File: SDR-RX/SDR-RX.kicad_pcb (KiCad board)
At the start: 2 copper layers, 53 x 51 mm, 50 parts, among them Q1 S8050, Q2 S8050, U1 Si4734-D60-GU, U2 ESP32-WROOM-32, U3 LD1117S33TR_SOT223, Y1 32.768kHz

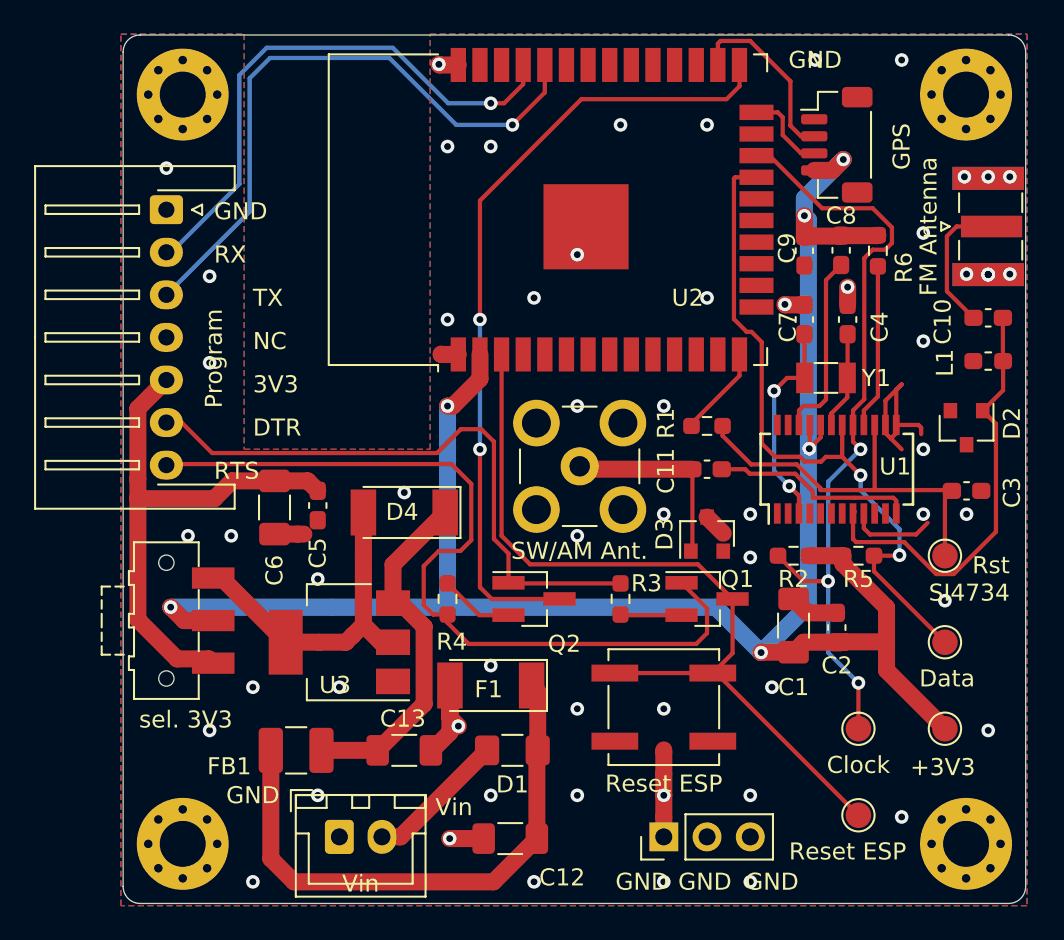
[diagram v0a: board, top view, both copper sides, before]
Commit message: changed footprint D1 & D4 due to assembly objection
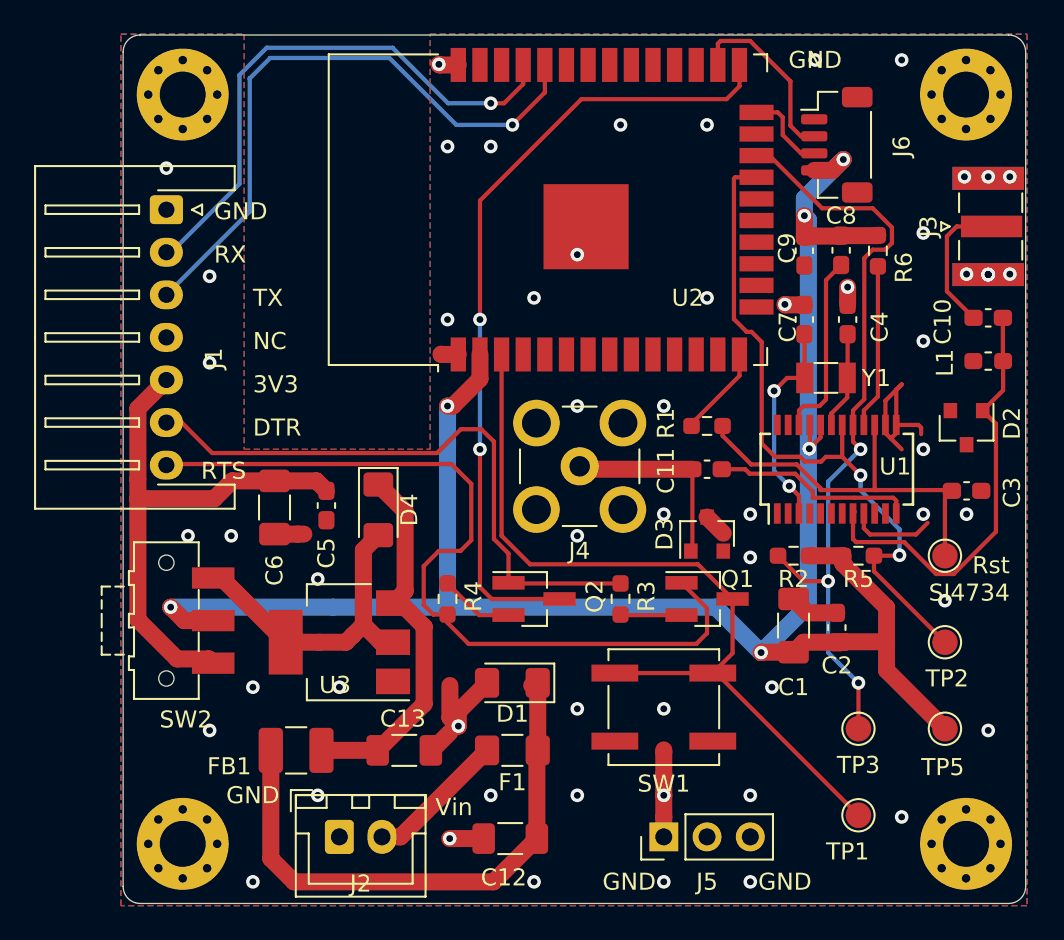
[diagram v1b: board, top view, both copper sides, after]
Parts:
- D1, D4: footprint Diode_SMD:D_MELF -> Diode_SMD:D_1206_3216Metric_Pad1.42x1.75mm_HandSolder
- J1: renamed from Program; value J1 -> Program
- J2: renamed from Vin ; value J2 -> Vin
- J3: renamed from FM Antenna; value J3 -> FM Antenna
- J4: renamed from SW/AM Ant.
- J6: renamed from GPS; value J6 -> GPS
- SW1: renamed from Reset ESP; value SW1 -> Reset ESP
- SW2: renamed from sel. 3V3 ; value SW2 -> 3V3 J5/J2
- TP1: renamed from Reset ESP
- TP4: renamed from Reset SI4734
- TP5: renamed from +3V3; value TP5 -> +3V3
- moved D4 1.53 mm to (125.2, 92.6), turned to 270 degrees
- moved D1 1.28 mm to (133.1, 102.8)
- moved C5 0.51 mm to (122.2, 92.4)
- renumbered GND to J5, Data to TP2, Clock to TP3
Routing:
- net Net-(C13-Pad1): track 20.7 -> 22.0 mm
- net Net-(C5-Pad1): track 32.0 -> 32.5 mm
- net GND: track 39.4 -> 39.8 mm, vias 60 -> 58

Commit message: changed Designator J5 to Program1 to avoid BPM/CPL missmatch on SMT assembly
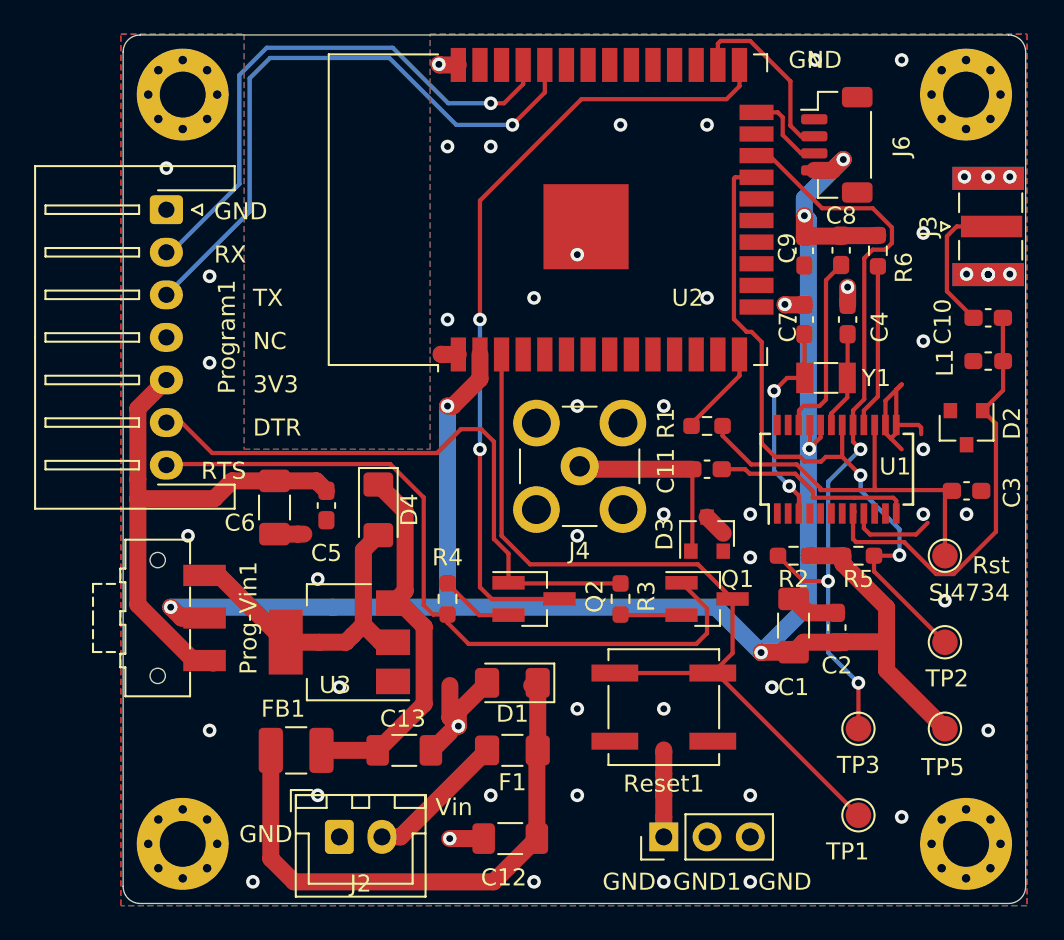
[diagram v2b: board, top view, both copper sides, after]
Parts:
- GND1: renamed from J5; value Conn_01x03_Male -> GND TP
- Prog-Vin1: renamed from SW2; value 3V3 J5/J2 -> SW2
- Program1: renamed from J1; value Program -> J1
- Reset1: renamed from SW1; value Reset ESP -> SW1
- moved Prog-Vin1 0.53 mm to (112.3, 99.0)
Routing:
- net Net-(Program1-Pad7): track 49.1 -> 44.0 mm
- net Net-(D4-Pad2): track 19.1 -> 20.8 mm
- net Net-(C5-Pad1): track 32.5 -> 31.8 mm
- net +3V3: track 118.8 -> 118.3 mm
- net GND: vias 58 -> 55

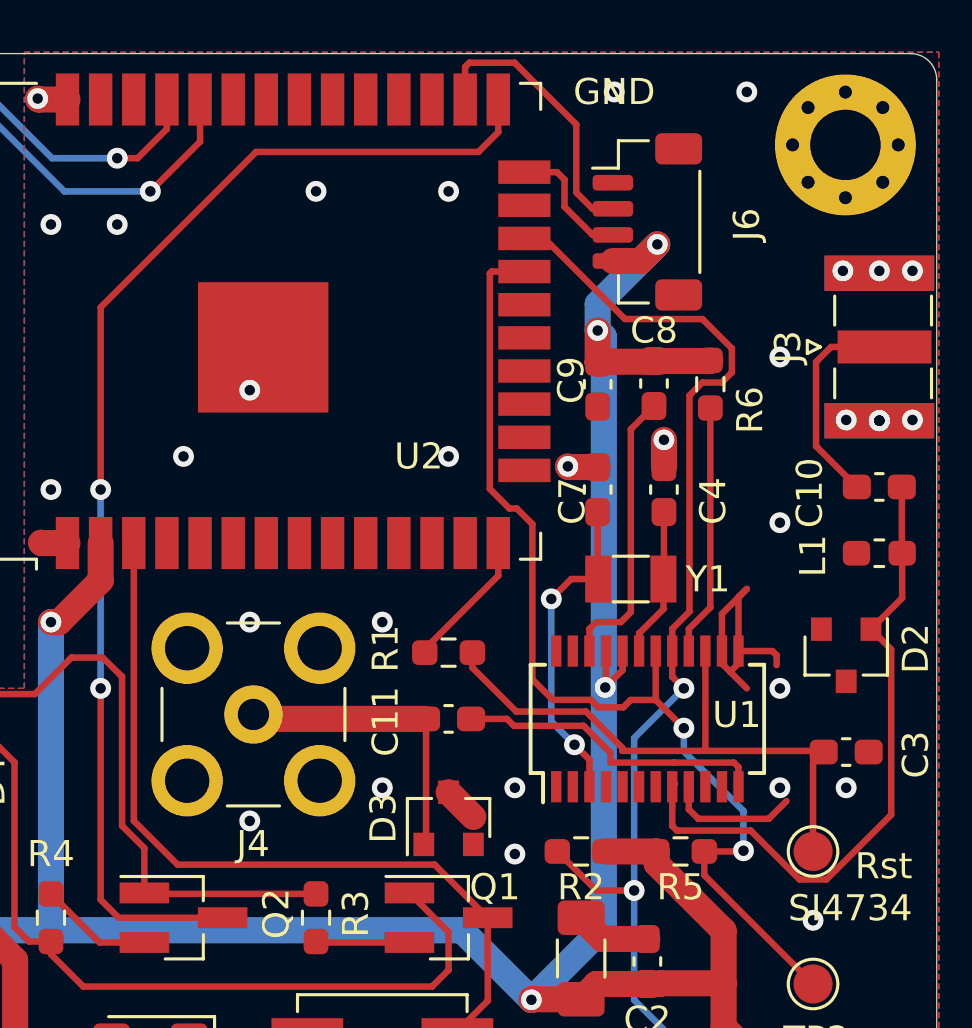
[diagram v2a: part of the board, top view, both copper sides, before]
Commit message: reversed remaining value/designator of all connectors
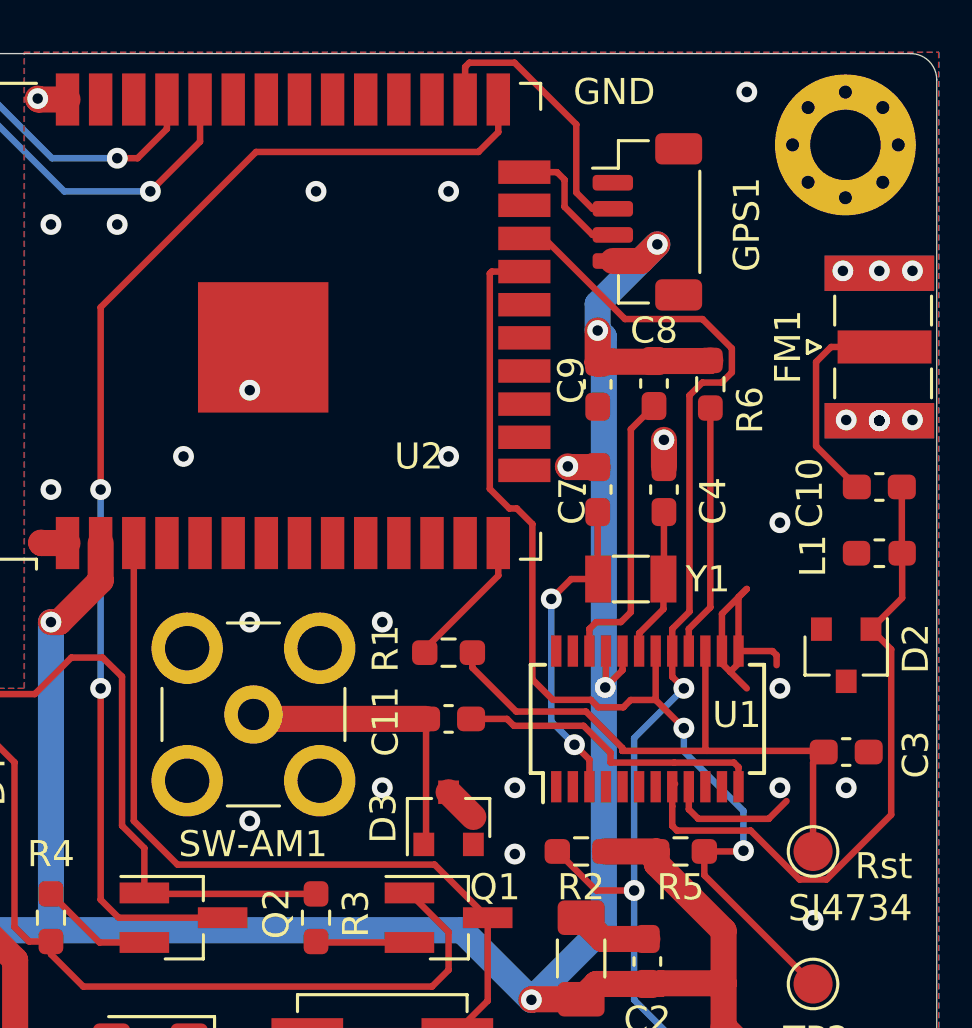
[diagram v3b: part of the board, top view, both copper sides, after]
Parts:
- FM1: renamed from J3; value FM Antenna -> J3
- GPS1: renamed from J6; value GPS -> J6
- SW-AM1: renamed from J4; value AM Antenna -> J4
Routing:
- net GND: vias 55 -> 53

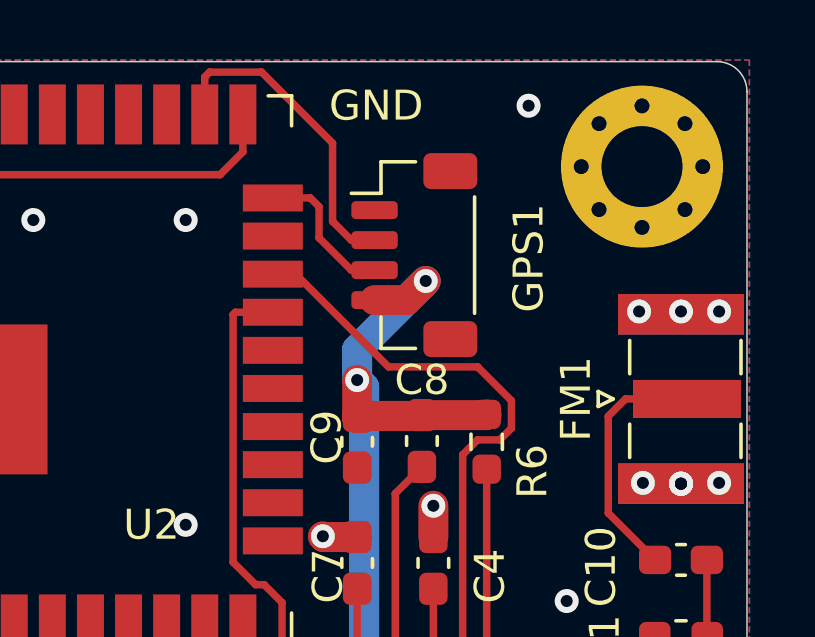
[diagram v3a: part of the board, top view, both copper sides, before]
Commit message: adapted footprint of GPS1/J6 to real footprint of SMT assembly, created hb9gvd.pretty directory
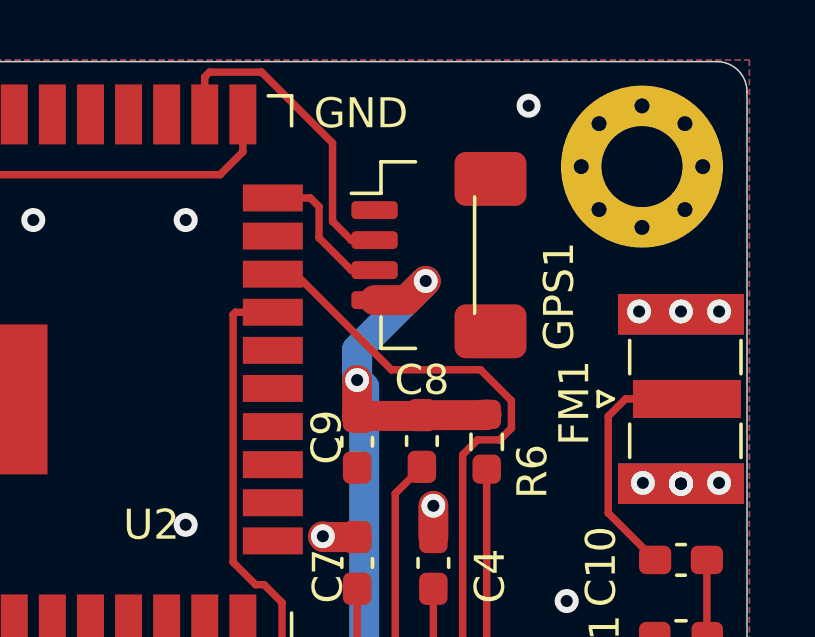
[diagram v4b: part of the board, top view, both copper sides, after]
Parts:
- GPS1: footprint Connector_JST:JST_SH_BM04B-SRSS-TB_1x04-1MP_P1.00mm_Vertical -> hb9gvd:JST_SH_BM04B-SRSS-TB_1x04-1MP_P1.00mm_Vertical-GPS
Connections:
- GPS1 pad MP: (no net) -> GND
